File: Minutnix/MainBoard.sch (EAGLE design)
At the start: 121 parts, among them IC3 TP4056, IC7 FT232RL, Q4 32.768kHz, X1 FH12-12S-0.5SH, X2 JST-XH-03-PIN-LONG-PAD, X4 JST-XH-03-PIN-LONG-PAD

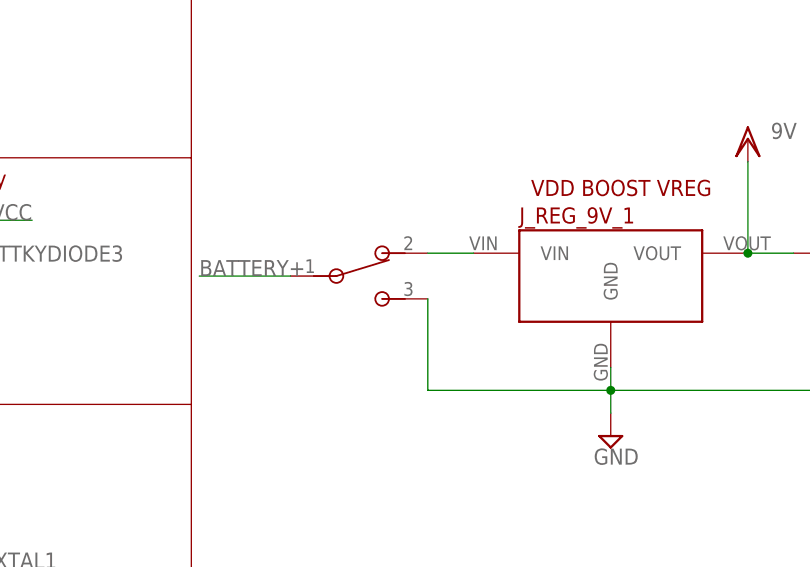
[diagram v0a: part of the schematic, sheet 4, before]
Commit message: libs actualisation + drc rules for expander
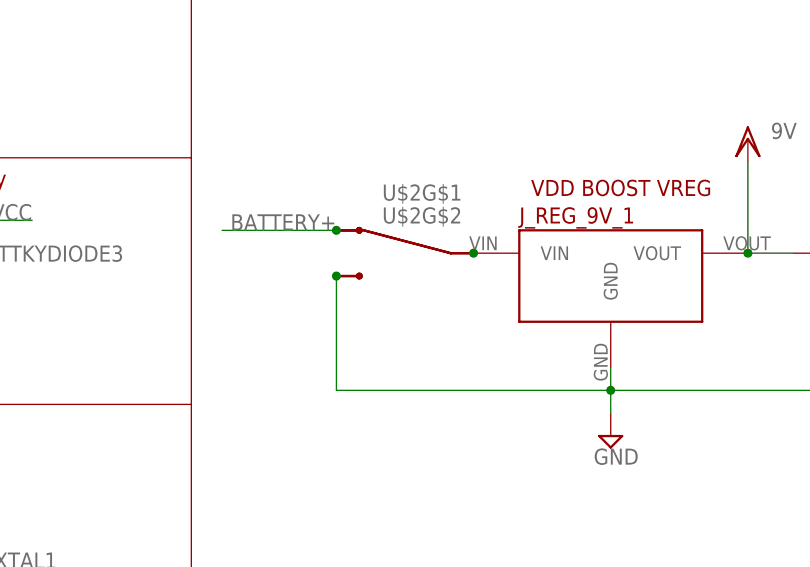
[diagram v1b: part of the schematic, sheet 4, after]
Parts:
- removed U$1: SW, MySwitch:SW
- added U$2: X2, Isostat:X2
- X1: value FH12-12S-0.5SH -> FH12-12S-0.5S_THINNER; device con-hirose:FH12-12S-0.5SH -> My_con-hirose:FH12-12S-0.5S_THINNER
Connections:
- removed net N$29: J_REG_9V_1.VIN, U$1.2
- new net N$81: J_REG_9V_1.VIN, U$2G$1.P$2, U$2G$2.P$2
- net BATTERY+: now also U$2G$1.P$1, U$2G$2.P$1; no longer U$1.1
- net GND: now also U$2G$1.P$3, U$2G$2.P$3; no longer U$1.3
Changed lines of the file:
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@@
 <part name="MSDIGIT_MINUTES" library="BigLED7Segm" deviceset="LED-7-SEGM-56MM" device=""/>
 <part name="R61" library="rcl" library_urn="urn:adsk.eagle:library:334" deviceset="R-EU_" device="R0603" package3d_urn="urn:adsk.eagle:package:23555/2" value="4.7k"/>
-<part name="X1" library="con-hirose" library_urn="urn:adsk.eagle:library:152" deviceset="FH12-12S-0.5S" device="H" package3d_urn="urn:adsk.eagle:package:7320/1"/>
+<part name="X1" library="My_con-hirose" deviceset="FH12-12S-0.5S_THINNER" device=""/>
 <part name="EXPANDER" library="i2c" deviceset="PCF8574" device="AT"/>
 <part name="SUPPLY1" library="supply2" library_urn="urn:adsk.eagle:library:372" deviceset="GND" device=""/>
@@
 <part name="SUPPLY16" library="supply2" library_urn="urn:adsk.eagle:library:372" deviceset="GND" device=""/>
 <part name="IC2" library="v-reg-2" deviceset="LM1117" device=""/>
-<part name="U$1" library="MySwitch" deviceset="SW" device=""/>
 <part name="SUPPLY6" library="supply2" library_urn="urn:adsk.eagle:library:372" deviceset="VCC" device=""/>
 <part name="C5SPRAWDZGOOOOOOOOOOOOOOOOOOOOOOOOOOOOOOOOOOOOOOOOOOO" library="rcl" library_urn="urn:adsk.eagle:library:334" deviceset="C-EU" device="C3216" package3d_urn="urn:adsk.eagle:package:23628/2" value="10u"/>
@@
 <part name="SUPPLY13" library="supply2" library_urn="urn:adsk.eagle:library:372" deviceset="GND" device=""/>
 <part name="C5SPRAWDZGOOOOOOOOOOOOOOOOOOOOOOOOOOOOOOOOOOOOOOOOOOO1" library="rcl" library_urn="urn:adsk.eagle:library:334" deviceset="C-EU" device="C3216" package3d_urn="urn:adsk.eagle:package:23628/2" value="10u"/>
+<part name="U$2" library="Isostat" deviceset="X2" device=""/>
 </parts>
 <sheets>
@@
 <attribute name="VALUE" x="144.78" y="53.34" size="1.778" layer="96"/>
 </instance>
-<instance part="U$1" gate="G$1" x="86.36" y="60.96" smashed="yes" rot="MR90"/>
 <instance part="SUPPLY6" gate="G$1" x="152.4" y="73.66" smashed="yes">
 <attribute name="VALUE" x="150.495" y="76.835" size="1.778" layer="96"/>
@@
 <attribute name="NAME" x="102.743" y="157.9626" size="1.778" layer="95"/>
 <attribute name="VALUE" x="100.203" y="137.6426" size="1.778" layer="96"/>
+</instance>
+<instance part="U$2" gate="G$1" x="91.44" y="63.5" smashed="yes" rot="MR270">
+<attribute name="NAME" x="88.9" y="71.12" size="1.778" layer="95" rot="MR180"/>
+</instance>
+<instance part="U$2" gate="G$2" x="91.44" y="63.5" smashed="yes" rot="MR270">
+<attribute name="NAME" x="88.9" y="68.58" size="1.778" layer="95" rot="MR180"/>
 </instance>
 </instances>
@@
 <wire x1="142.24" y1="48.26" x2="114.3" y2="48.26" width="0.1524" layer="91"/>
 <junction x="114.3" y="48.26"/>
-<pinref part="U$1" gate="G$1" pin="3"/>
-<wire x1="93.98" y1="58.42" x2="93.98" y2="48.26" width="0.1524" layer="91"/>
-<wire x1="93.98" y1="48.26" x2="114.3" y2="48.26" width="0.1524" layer="91"/>
+<wire x1="83.82" y1="48.26" x2="114.3" y2="48.26" width="0.1524" layer="91"/>
 <pinref part="C5SPRAWDZGOOOOOOOOOOOOOOOOOOOOOOOOOOOOOOOOOOOOOOOOOOO" gate="G$1" pin="2"/>
 <wire x1="142.24" y1="48.26" x2="152.4" y2="48.26" width="0.1524" layer="91"/>
 <wire x1="152.4" y1="48.26" x2="152.4" y2="50.8" width="0.1524" layer="91"/>
 <junction x="142.24" y="48.26"/>
+<pinref part="U$2" gate="G$1" pin="P$3"/>
+<pinref part="U$2" gate="G$2" pin="P$3"/>
+<wire x1="83.82" y1="48.26" x2="83.82" y2="60.96" width="0.1524" layer="91"/>
+<junction x="83.82" y="60.96"/>
 </segment>
 <segment>
@@
 <net name="BATTERY+" class="0">
 <segment>
-<pinref part="U$1" gate="G$1" pin="1"/>
-<wire x1="78.74" y1="60.96" x2="68.58" y2="60.96" width="0.1524" layer="91"/>
-<label x="68.58" y="60.96" size="1.778" layer="95"/>
-</segment>
-<segment>
 <pinref part="IC3" gate="G$1" pin="BAT"/>
 <pinref part="X2" gate="-1" pin="S"/>
@@
 <label x="154.94" y="142.24" size="1.778" layer="95"/>
 </segment>
+<segment>
+<pinref part="U$2" gate="G$1" pin="P$1"/>
+<pinref part="U$2" gate="G$2" pin="P$1"/>
+<wire x1="83.82" y1="66.04" x2="71.12" y2="66.04" width="0.1524" layer="91"/>
+<junction x="83.82" y="66.04"/>
+<label x="83.82" y="66.04" size="1.778" layer="95" rot="MR0"/>
+</segment>
 </net>
 <net name="BATTERY_S" class="0">
@@
 </segment>
 </net>
-<net name="N$29" class="0">
-<segment>
-<pinref part="J_REG_9V_1" gate="J_REG_9V" pin="VIN"/>
-<pinref part="U$1" gate="G$1" pin="2"/>
-<wire x1="93.98" y1="63.5" x2="99.06" y2="63.5" width="0.1524" layer="91"/>
-</segment>
-</net>
 <net name="N$52" class="0">
 <segment>
@@
 </segment>
 </net>
+<net name="N$81" class="0">
+<segment>
+<pinref part="U$2" gate="G$1" pin="P$2"/>
+<pinref part="U$2" gate="G$2" pin="P$2"/>
+<pinref part="J_REG_9V_1" gate="J_REG_9V" pin="VIN"/>
+<junction x="99.06" y="63.5"/>
+</segment>
+</net>

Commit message: Consolidation of schematic + lib restore
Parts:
- SHOTTKYDIODE3: device s2x_10:S2A -> Shottky:S2A
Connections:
- net AVCC: now also L1.2, R57.S; no longer L1.1, R57.A
- net LIGHT_SENS: now also R57.E; no longer R57.S
- net S_VCC: now also L1.1; no longer L1.2
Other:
- note added: "ATMEGA 328P"
- note added: "OUTPUTS"
- note added: "REGISTERS AND EXPANDER SUPPLY PORTS"
- note added: "SUPPLY AND AREF"
- note added: "UNUSED PINS JUMPERS"
- note removed: "ACTUATORS"
- note removed: "AVCC Supply and AREF"
- note removed: "Atmega328p version"
- note removed: "Atmega8 version"
- note removed: "CONTROL"
- note removed: "DISPLAY SUPPLY PORTS"
- note removed: "INPUTS"
- note removed: "Unused pins jumpers"
- note removed: "VCC Logic supply"

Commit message: lib update + board ongoing
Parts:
- removed SJ1: (no value), jumper:SJ
- Q4: device crystal_clock:CRYSTAL-32.768KHZSMD-2X6 -> crystal_clock:CRYSTAL-32.768KHZ_GNDSMD-2X6
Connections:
- removed net N$30: R61.2, SJ1.2
- removed net N$50: COLON1.C, R32.1
- removed net N$51: COLON2.C, R35.1
- new net N$29: COLON2.A, R34.2
- new net N$56: COLON1.A, R50.2
- net BATTERY+: now also C5SPRAWDZGOOOOOOOOOOOOOOOOOOOOOOOOOOOOOOOOOOOOOOOOOOO1.2
- net GND: now also Q4.GND, U$2CASE1.P$1, U$2CASE2.P$1; no longer C5SPRAWDZGOOOOOOOOOOOOOOOOOOOOOOOOOOOOOOOOOOOOOOOOOOO1.2, PHOTORES.1
- net GNDA: now also PHOTORES.1
- net N$2: now also COLON1.C; no longer R50.2
- net N$20: now also COLON2.C; no longer R34.2
- net UP1: now also R61.2; no longer SJ1.1
- net VCC: now also R32.1, R35.1; no longer COLON1.A, COLON2.A
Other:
- moved on the sheet: C5SPRAWDZGOOOOOOOOOOOOOOOOOOOOOOOOOOOOOOOOOOOOOOOOOOO1, COLON1, COLON2

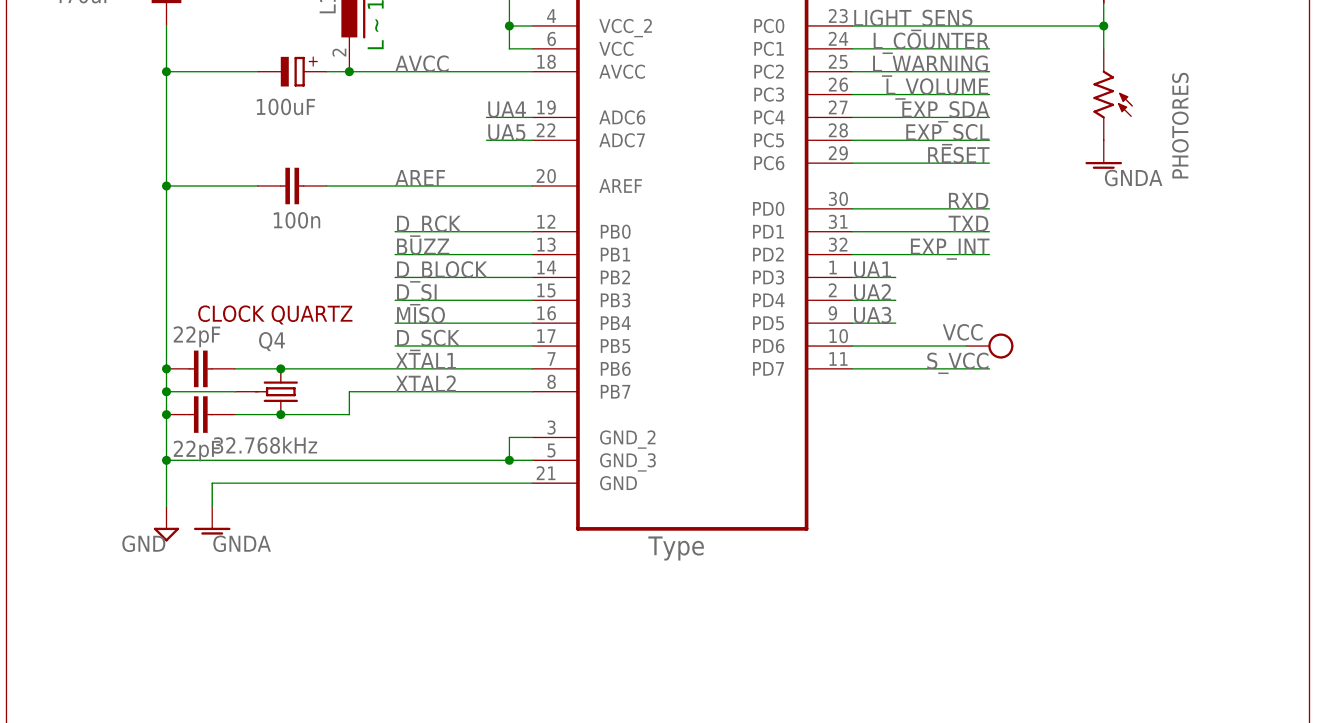
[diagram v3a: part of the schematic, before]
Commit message: PCB with original pinout
Register inputs unconnected but drawn close
Not every path has optimal width
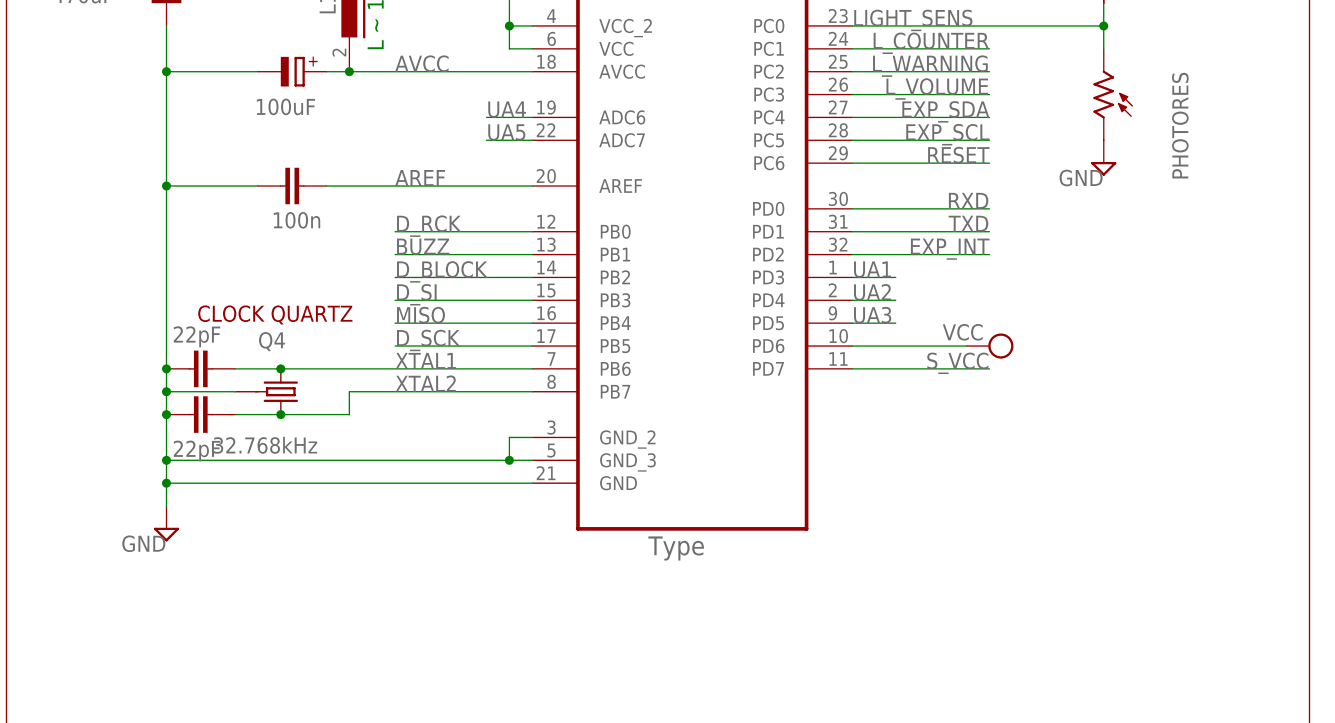
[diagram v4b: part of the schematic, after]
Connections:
- removed net GNDA: ATMEGA328P.GND, PHOTORES.1
- net GND: now also ATMEGA328P.GND, PHOTORES.1
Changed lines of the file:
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@@
 <part name="R47" library="rcl" library_urn="urn:adsk.eagle:library:334" deviceset="R-EU_" device="R0603" package3d_urn="urn:adsk.eagle:package:23555/2" value="620R-1k"/>
 <part name="R52" library="rcl" library_urn="urn:adsk.eagle:library:334" deviceset="R-EU_" device="R0603" package3d_urn="urn:adsk.eagle:package:23555/2" value="620R-1k"/>
-<part name="GND2" library="supply1" library_urn="urn:adsk.eagle:library:371" deviceset="GNDA" device=""/>
 <part name="C4" library="rcl" library_urn="urn:adsk.eagle:library:334" deviceset="C-EU" device="C0603" package3d_urn="urn:adsk.eagle:package:23616/2" value="100n"/>
 <part name="R56" library="rcl" library_urn="urn:adsk.eagle:library:334" deviceset="R-EU_" device="R0603" package3d_urn="urn:adsk.eagle:package:23555/2" value="4.7k"/>
@@
 <part name="SUPPLY16" library="supply2" library_urn="urn:adsk.eagle:library:372" deviceset="GND" device=""/>
 <part name="FRAME1" library="frames" library_urn="urn:adsk.eagle:library:229" deviceset="A3L-LOC" device=""/>
-<part name="GND1" library="supply1" library_urn="urn:adsk.eagle:library:371" deviceset="GNDA" device=""/>
 <part name="C5SPRAWDZGOOOOOOOOOOOOOOOOOOOOOOOOOOOOOOOOOOOOOOOOOOO1" library="rcl" library_urn="urn:adsk.eagle:library:334" deviceset="C-EU" device="C3216" package3d_urn="urn:adsk.eagle:package:23628/2" value="10u"/>
+<part name="SUPPLY3" library="supply2" library_urn="urn:adsk.eagle:library:372" deviceset="GND" device=""/>
 </parts>
 <sheets>
@@
 <attribute name="VALUE" x="90.805" y="5.715" size="1.778" layer="96" rot="MR0"/>
 </instance>
-<instance part="GND2" gate="1" x="5.08" y="-15.24" smashed="yes">
-<attribute name="VALUE" x="5.08" y="-17.78" size="1.778" layer="96"/>
-</instance>
 <instance part="LSDIGIT_SECONDS" gate="G$1" x="246.38" y="91.44" smashed="yes" rot="R270">
 <attribute name="NAME" x="241.3" y="100.965" size="1.778" layer="95"/>
@@
 <instance part="U$2" gate="CASE1" x="-17.78" y="142.24" smashed="yes" rot="R90"/>
 <instance part="U$2" gate="CASE2" x="-12.7" y="142.24" smashed="yes" rot="R90"/>
-<instance part="GND1" gate="1" x="104.14" y="25.4" smashed="yes">
-<attribute name="VALUE" x="104.14" y="22.86" size="1.778" layer="96"/>
-</instance>
 <instance part="C5SPRAWDZGOOOOOOOOOOOOOOOOOOOOOOOOOOOOOOOOOOOOOOOOOOO1" gate="G$1" x="-27.94" y="190.5" smashed="yes">
 <attribute name="NAME" x="-34.036" y="142.621" size="1.778" layer="95"/>
 <attribute name="VALUE" x="-34.036" y="188.341" size="1.778" layer="96"/>
+</instance>
+<instance part="SUPPLY3" gate="GND" x="104.14" y="25.4" smashed="yes" rot="MR0">
+<attribute name="VALUE" x="104.14" y="22.86" size="1.778" layer="96" rot="MR0"/>
 </instance>
 </instances>
@@
 <junction x="0" y="-2.54"/>
 <pinref part="SUPPLY38" gate="GND" pin="GND"/>
-<wire x1="0" y1="-12.7" x2="0" y2="-7.62" width="0.1524" layer="91"/>
+<wire x1="0" y1="-12.7" x2="0" y2="-10.16" width="0.1524" layer="91"/>
 <junction x="0" y="-7.62"/>
 <pinref part="Q4" gate="G$1" pin="GND"/>
+<wire x1="0" y1="-10.16" x2="0" y2="-7.62" width="0.1524" layer="91"/>
 <wire x1="7.62" y1="0" x2="0" y2="0" width="0.1524" layer="91"/>
 <junction x="0" y="0"/>
+<pinref part="ATMEGA328P" gate="A" pin="GND"/>
+<wire x1="40.64" y1="-10.16" x2="0" y2="-10.16" width="0.1524" layer="91"/>
+<junction x="0" y="-10.16"/>
 </segment>
 <segment>
@@
 <junction x="-15.24" y="137.16"/>
 </segment>
+<segment>
+<pinref part="SUPPLY3" gate="GND" pin="GND"/>
+<pinref part="PHOTORES" gate="G$1" pin="1"/>
+</segment>
 </net>
 <net name="L_COUNTER" class="0">
@@
 </segment>
 </net>
-<net name="GNDA" class="0">
-<segment>
-<pinref part="ATMEGA328P" gate="A" pin="GND"/>
-<wire x1="40.64" y1="-10.16" x2="5.08" y2="-10.16" width="0.1524" layer="91"/>
-<wire x1="5.08" y1="-10.16" x2="5.08" y2="-12.7" width="0.1524" layer="91"/>
-<pinref part="GND2" gate="1" pin="GNDA"/>
-</segment>
-<segment>
-<pinref part="GND1" gate="1" pin="GNDA"/>
-<pinref part="PHOTORES" gate="G$1" pin="1"/>
-</segment>
-</net>
